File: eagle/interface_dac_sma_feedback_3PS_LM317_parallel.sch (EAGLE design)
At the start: 38 parts, among them IC1 ISO1540, X1 BU-SMA-V

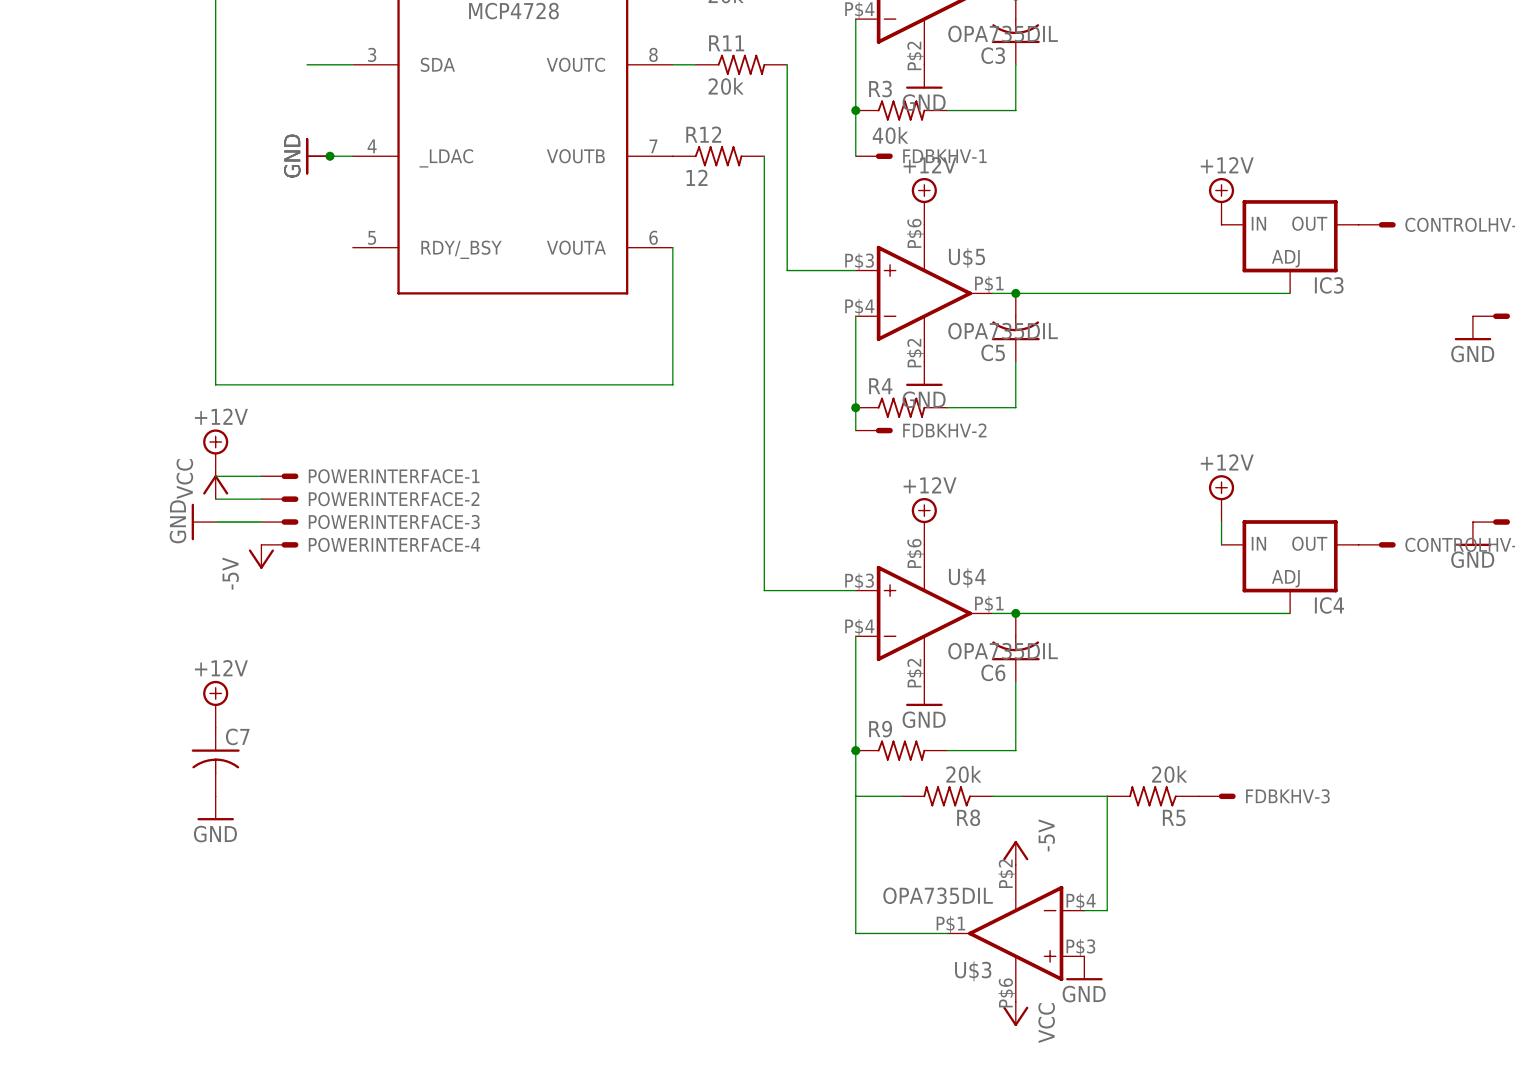
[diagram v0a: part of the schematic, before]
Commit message: two ps in parallel
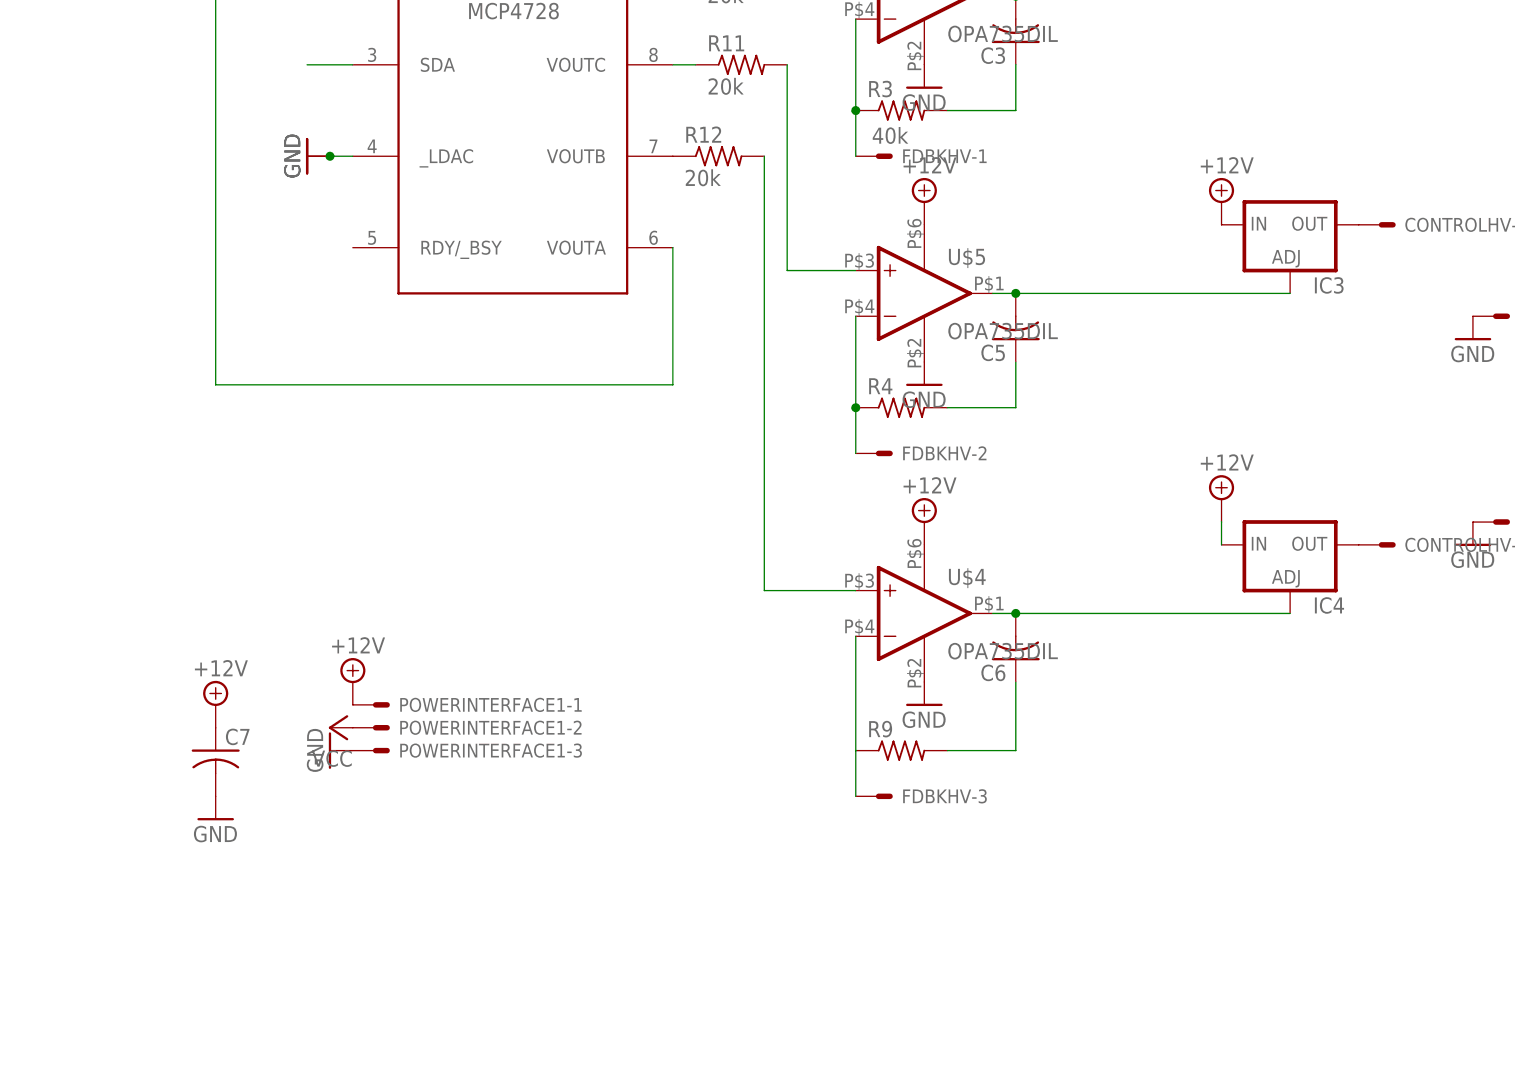
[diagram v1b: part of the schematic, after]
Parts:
- removed POWERINTERFACE: (no value), con-molex:KK-156-4
- removed R5, R8: 20k, resistor:R-US_0207/12
- removed U$3: OPA735DIL, texas:OPA735DIL
- added POWERINTERFACE1: (no value), con-molex:KK-156-3
- R12: value 12 -> 20k
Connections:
- removed net -5V: POWERINTERFACE-4.S, U$3.V-
- removed net N$23: R5.2, R8.1, U$3.-IN
- removed net N$9: FDBKHV-3.S, R5.1
- net +12V: now also POWERINTERFACE1-1.S; no longer POWERINTERFACE-1.S
- net GND: now also POWERINTERFACE1-3.S; no longer POWERINTERFACE-3.S, U$3.+IN
- net N$14: now also FDBKHV-3.S; no longer R8.2, U$3.OUT
- net VCC: now also POWERINTERFACE1-2.S; no longer POWERINTERFACE-2.S, U$3.V+
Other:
- moved on the sheet: FDBKHV-2, FDBKHV-3
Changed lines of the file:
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@@
 <parts>
 <part name="PCB1" library="E14_Arduino_published" deviceset="ARDUINO_MICRO" device=""/>
-<part name="P+5" library="supply1" deviceset="VCC" device=""/>
-<part name="GND4" library="supply1" deviceset="GND" device=""/>
-<part name="P+2" library="supply2" deviceset="+12V" device=""/>
 <part name="U$1" library="linear-technology" deviceset="LTC6992" device=""/>
 <part name="C4" library="resistor" deviceset="C-US" device="075-063X106"/>
@@
 <part name="GND2" library="supply1" deviceset="GND" device=""/>
 <part name="GND6" library="supply1" deviceset="GND" device=""/>
-<part name="POWERINTERFACE" library="con-molex" deviceset="KK-156-4" device=""/>
-<part name="P-1" library="supply1" deviceset="-5V" device=""/>
-<part name="R5" library="resistor" deviceset="R-US_" device="0207/12" value="20k"/>
-<part name="R8" library="resistor" deviceset="R-US_" device="0207/12" value="20k"/>
-<part name="P-2" library="supply1" deviceset="-5V" device=""/>
-<part name="P+13" library="supply1" deviceset="VCC" device=""/>
-<part name="GND18" library="supply1" deviceset="GND" device=""/>
-<part name="U$3" library="texas" deviceset="OPA735" device="DIL"/>
 <part name="U$4" library="texas" deviceset="OPA735" device="DIL"/>
 <part name="U$5" library="texas" deviceset="OPA735" device="DIL"/>
@@
 <part name="R10" library="resistor" deviceset="R-US_" device="0207/12" value="20k"/>
 <part name="R11" library="resistor" deviceset="R-US_" device="0207/12" value="20k"/>
-<part name="R12" library="resistor" deviceset="R-US_" device="0207/12" value="12"/>
+<part name="R12" library="resistor" deviceset="R-US_" device="0207/12" value="20k"/>
+<part name="POWERINTERFACE1" library="con-molex" deviceset="KK-156-3" device=""/>
+<part name="P+13" library="supply2" deviceset="+12V" device=""/>
+<part name="P+15" library="supply1" deviceset="VCC" device=""/>
+<part name="GND18" library="supply1" deviceset="GND" device=""/>
 </parts>
 <sheets>
@@
 <instances>
 <instance part="PCB1" gate="G$1" x="27.94" y="81.28"/>
-<instance part="P+5" gate="VCC" x="88.9" y="38.1"/>
-<instance part="GND4" gate="1" x="86.36" y="33.02" rot="R270"/>
-<instance part="P+2" gate="+12V" x="88.9" y="40.64"/>
 <instance part="U$1" gate="G$1" x="266.7" y="109.22"/>
 <instance part="C4" gate="G$1" x="294.64" y="83.82"/>
@@
 <instance part="CONTROLHV" gate="-4" x="231.14" y="55.88"/>
 <instance part="FDBKHV" gate="-1" x="162.56" y="73.66"/>
-<instance part="FDBKHV" gate="-2" x="162.56" y="43.18"/>
-<instance part="FDBKHV" gate="-3" x="200.66" y="2.54"/>
+<instance part="FDBKHV" gate="-2" x="162.56" y="40.64"/>
+<instance part="FDBKHV" gate="-3" x="162.56" y="2.54"/>
 <instance part="FDBKHV" gate="-4" x="231.14" y="33.02"/>
 <instance part="GND2" gate="1" x="228.6" y="53.34"/>
 <instance part="GND6" gate="1" x="228.6" y="30.48"/>
-<instance part="POWERINTERFACE" gate="-1" x="96.52" y="38.1"/>
-<instance part="POWERINTERFACE" gate="-2" x="96.52" y="35.56"/>
-<instance part="POWERINTERFACE" gate="-3" x="96.52" y="33.02"/>
-<instance part="POWERINTERFACE" gate="-4" x="96.52" y="30.48"/>
-<instance part="P-1" gate="1" x="93.98" y="27.94"/>
-<instance part="R5" gate="G$1" x="193.04" y="2.54" rot="R180"/>
-<instance part="R8" gate="G$1" x="170.18" y="2.54" rot="R180"/>
-<instance part="P-2" gate="1" x="177.8" y="-2.54" rot="R180"/>
-<instance part="P+13" gate="VCC" x="177.8" y="-22.86" rot="R180"/>
-<instance part="GND18" gate="1" x="185.42" y="-17.78"/>
-<instance part="U$3" gate="G$1" x="177.8" y="-12.7" rot="R180"/>
 <instance part="U$4" gate="G$1" x="167.64" y="22.86"/>
 <instance part="U$5" gate="G$1" x="167.64" y="58.42"/>
@@
 <instance part="R11" gate="G$1" x="147.32" y="83.82"/>
 <instance part="R12" gate="G$1" x="144.78" y="73.66"/>
+<instance part="POWERINTERFACE1" gate="-1" x="106.68" y="12.7"/>
+<instance part="POWERINTERFACE1" gate="-2" x="106.68" y="10.16"/>
+<instance part="POWERINTERFACE1" gate="-3" x="106.68" y="7.62"/>
+<instance part="P+13" gate="+12V" x="104.14" y="15.24"/>
+<instance part="P+15" gate="VCC" x="101.6" y="10.16" rot="R90"/>
+<instance part="GND18" gate="1" x="101.6" y="7.62" rot="R270"/>
 </instances>
 <busses>
@@
 <nets>
 <net name="GND" class="0">
-<segment>
-<wire x1="93.98" y1="33.02" x2="88.9" y2="33.02" width="0.1524" layer="91"/>
-<pinref part="GND4" gate="1" pin="GND"/>
-<pinref part="POWERINTERFACE" gate="-3" pin="S"/>
-</segment>
 <segment>
 <pinref part="R16" gate="G$1" pin="A"/>
@@
 </segment>
 <segment>
-<pinref part="GND18" gate="1" pin="GND"/>
-<pinref part="U$3" gate="G$1" pin="+IN"/>
-</segment>
-<segment>
 <pinref part="GND19" gate="1" pin="GND"/>
 <pinref part="U$4" gate="G$1" pin="V-"/>
@@
 <pinref part="GND20" gate="1" pin="GND"/>
 </segment>
+<segment>
+<pinref part="POWERINTERFACE1" gate="-3" pin="S"/>
+<pinref part="GND18" gate="1" pin="GND"/>
+</segment>
 </net>
 <net name="PWM6" class="0">
@@
 </net>
 <net name="VCC" class="0">
-<segment>
-<wire x1="93.98" y1="35.56" x2="88.9" y2="35.56" width="0.1524" layer="91"/>
-<pinref part="P+5" gate="VCC" pin="VCC"/>
-<pinref part="POWERINTERFACE" gate="-2" pin="S"/>
-</segment>
 <segment>
 <pinref part="U$1" gate="G$1" pin="P$5"/>
@@
 </segment>
 <segment>
-<pinref part="P+13" gate="VCC" pin="VCC"/>
-<pinref part="U$3" gate="G$1" pin="V+"/>
+<pinref part="POWERINTERFACE1" gate="-2" pin="S"/>
+<pinref part="P+15" gate="VCC" pin="VCC"/>
 </segment>
 </net>
@@
 <net name="+12V" class="0">
 <segment>
-<pinref part="P+2" gate="+12V" pin="+12V"/>
-<wire x1="88.9" y1="38.1" x2="93.98" y2="38.1" width="0.1524" layer="91"/>
-<pinref part="POWERINTERFACE" gate="-1" pin="S"/>
-</segment>
-<segment>
 <pinref part="P+3" gate="+12V" pin="+12V"/>
 <pinref part="IC2" gate="1" pin="IN"/>
@@
 <pinref part="P+14" gate="+12V" pin="+12V"/>
 <pinref part="C7" gate="G$1" pin="1"/>
+</segment>
+<segment>
+<pinref part="POWERINTERFACE1" gate="-1" pin="S"/>
+<pinref part="P+13" gate="+12V" pin="+12V"/>
 </segment>
 </net>
@@
 <net name="N$14" class="0">
 <segment>
-<wire x1="170.18" y1="-12.7" x2="160.02" y2="-12.7" width="0.1524" layer="91"/>
-<wire x1="160.02" y1="-12.7" x2="160.02" y2="2.54" width="0.1524" layer="91"/>
-<pinref part="R8" gate="G$1" pin="2"/>
+<wire x1="160.02" y1="7.62" x2="160.02" y2="20.32" width="0.1524" layer="91"/>
+<pinref part="U$4" gate="G$1" pin="-IN"/>
+<pinref part="R9" gate="G$1" pin="1"/>
+<pinref part="FDBKHV" gate="-3" pin="S"/>
 <wire x1="160.02" y1="2.54" x2="160.02" y2="7.62" width="0.1524" layer="91"/>
-<wire x1="160.02" y1="7.62" x2="160.02" y2="20.32" width="0.1524" layer="91"/>
-<wire x1="165.1" y1="2.54" x2="160.02" y2="2.54" width="0.1524" layer="91"/>
-<pinref part="U$4" gate="G$1" pin="-IN"/>
-<pinref part="U$3" gate="G$1" pin="OUT"/>
-<pinref part="R9" gate="G$1" pin="1"/>
-<junction x="160.02" y="7.62"/>
 </segment>
 </net>
@@
 <pinref part="U$5" gate="G$1" pin="-IN"/>
 <pinref part="R4" gate="G$1" pin="1"/>
-<wire x1="160.02" y1="45.72" x2="160.02" y2="43.18" width="0.1524" layer="91"/>
+<wire x1="160.02" y1="45.72" x2="160.02" y2="40.64" width="0.1524" layer="91"/>
 <junction x="160.02" y="45.72"/>
 </segment>
@@
 </segment>
 </net>
-<net name="-5V" class="0">
-<segment>
-<pinref part="POWERINTERFACE" gate="-4" pin="S"/>
-<pinref part="P-1" gate="1" pin="-5V"/>
-</segment>
-<segment>
-<pinref part="P-2" gate="1" pin="-5V"/>
-<pinref part="U$3" gate="G$1" pin="V-"/>
-</segment>
-</net>
-<net name="N$9" class="0">
-<segment>
-<pinref part="R5" gate="G$1" pin="1"/>
-<pinref part="FDBKHV" gate="-3" pin="S"/>
-</segment>
-</net>
-<net name="N$23" class="0">
-<segment>
-<pinref part="R5" gate="G$1" pin="2"/>
-<wire x1="187.96" y1="2.54" x2="187.96" y2="-10.16" width="0.1524" layer="91"/>
-<wire x1="187.96" y1="-10.16" x2="185.42" y2="-10.16" width="0.1524" layer="91"/>
-<pinref part="R8" gate="G$1" pin="1"/>
-<wire x1="187.96" y1="2.54" x2="175.26" y2="2.54" width="0.1524" layer="91"/>
-<pinref part="U$3" gate="G$1" pin="-IN"/>
-</segment>
-</net>
